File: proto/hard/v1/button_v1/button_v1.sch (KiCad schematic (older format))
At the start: 35 parts, among them J10 Conn_01x04_Male, J14 K3-2235D, J7 Conn_01x04_Female, J9 Conn_01x06_Male, Q1 TP0610T, Q3 TP0610T, Q8 IRLML2803, U1 LCD_2.8_SPI, U11 TC305, U12 LCD_1_8_SPI, U2 STM32F103C8Tx, Y1 8MHz

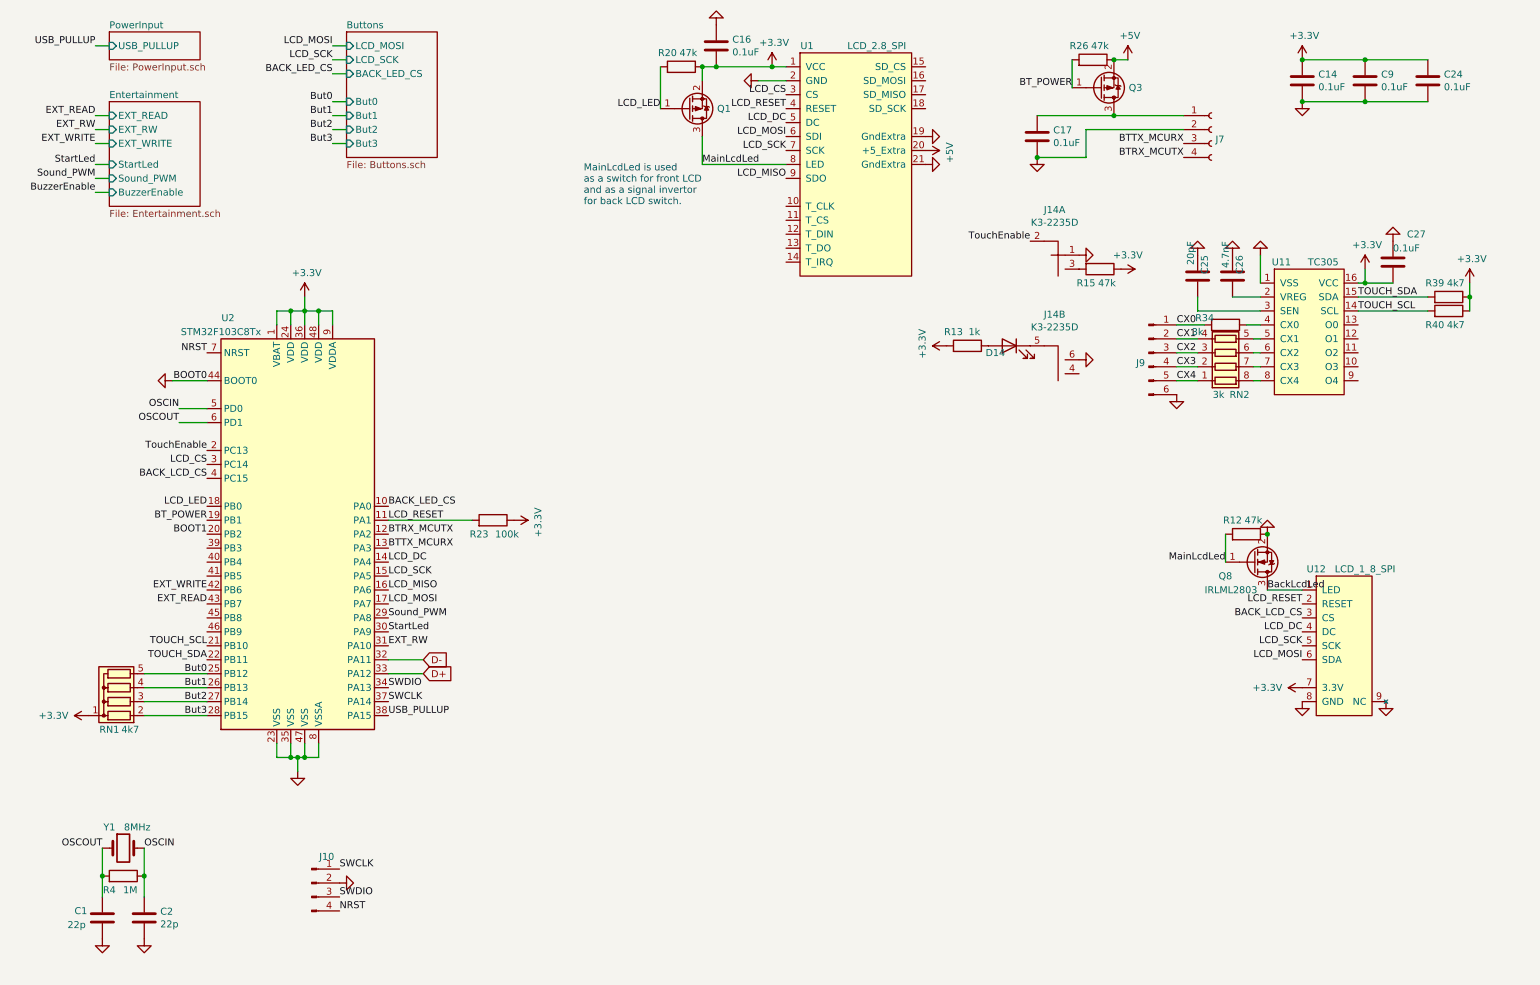
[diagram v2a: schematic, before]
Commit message: Debug connector updates: - added +3.3 connection - pins reorganized to match ST Link layout
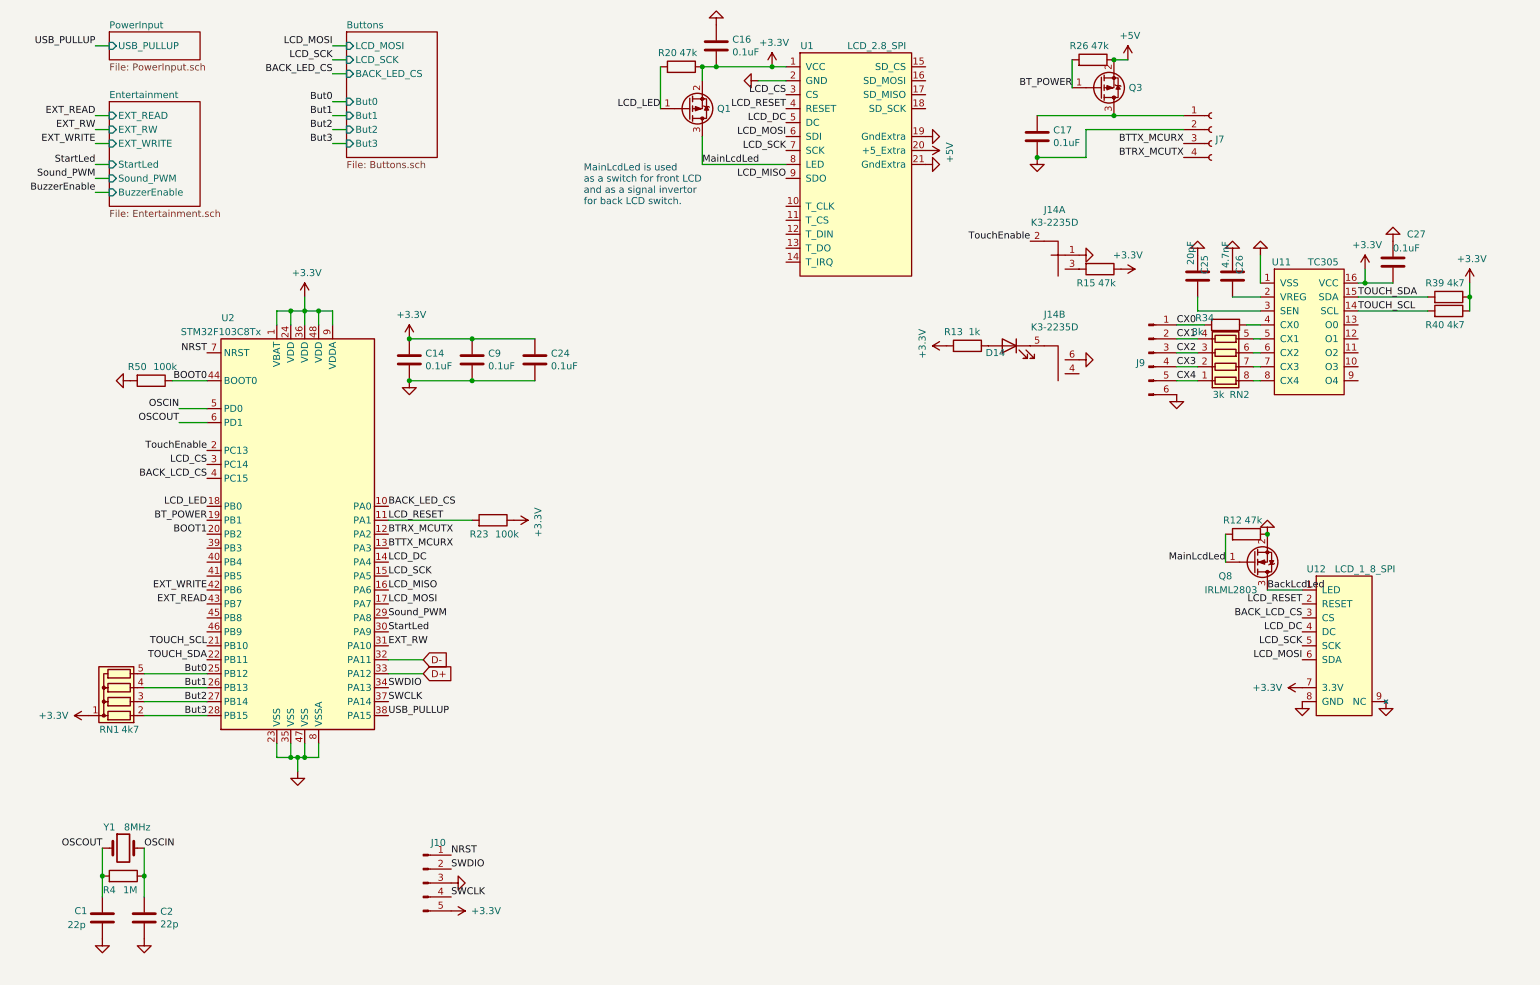
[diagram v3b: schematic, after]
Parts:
- removed J10: Conn_01x04_Male, Connector_PinHeader_2.54mm:PinHeader_1x04_P2.54mm_Vertical, symbol Connector:Conn_01x04_Male
- added J10: Conn_01x05_Male, Connector_PinHeader_2.54mm:PinHeader_1x05_P2.54mm_Vertical, symbol Connector:Conn_01x05_Male
- added R50: 100k, Resistor_SMD:R_0805_2012Metric_Pad1.15x1.40mm_HandSolder, symbol Device:R
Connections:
- net +3V3: now also J10.5 (Pin_5)
- net GND: now also J10.3 (Pin_3), R50.2; no longer U2.44 (BOOT0)
- net NRST: now also J10.1 (Pin_1)
- net SWCLK: now also J10.4 (Pin_4)
- net SWDIO: now also J10.2 (Pin_2)
- new net BOOT0: R50.1, U2.44 (BOOT0)
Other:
- moved on the sheet: C14, C24, C9
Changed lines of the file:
@@
 L power:GND #PWR036
 U 1 1 5D0E3AE6
-P 9700 1200
-F 0 "#PWR036" H 9700 950 50  0001 C CNN
-F 1 "GND" H 9705 1027 50  0001 C CNN
-F 2 "" H 9700 1200 50  0001 C CNN
-F 3 "" H 9700 1200 50  0001 C CNN
-	1    9700 1200
-	1    0    0    -1
-$EndComp
-Wire Wire Line
-	10150 1200 9700 1200
-Wire Wire Line
-	10150 1200 10600 1200
-Connection ~ 10150 1200
+P 3300 3200
+F 0 "#PWR036" H 3300 2950 50  0001 C CNN
+F 1 "GND" H 3305 3027 50  0001 C CNN
+F 2 "" H 3300 3200 50  0001 C CNN
+F 3 "" H 3300 3200 50  0001 C CNN
+	1    3300 3200
+	1    0    0    -1
+$EndComp
+Wire Wire Line
+	3750 3200 3300 3200
+Wire Wire Line
+	3750 3200 4200 3200
+Connection ~ 3750 3200
 $Comp
 L Device:C C14
 U 1 1 5D0E1987
-P 9700 1050
-F 0 "C14" H 9815 1096 50  0000 L CNN
-F 1 "0.1uF" H 9815 1005 50  0000 L CNN
-F 2 "Capacitor_SMD:C_0805_2012Metric_Pad1.15x1.40mm_HandSolder" H 9738 900 50  0001 C CNN
-F 3 "~" H 9700 1050 50  0001 C CNN
-	1    9700 1050
+P 3300 3050
+F 0 "C14" H 3415 3096 50  0000 L CNN
+F 1 "0.1uF" H 3415 3005 50  0000 L CNN
+F 2 "Capacitor_SMD:C_0805_2012Metric_Pad1.15x1.40mm_HandSolder" H 3338 2900 50  0001 C CNN
+F 3 "~" H 3300 3050 50  0001 C CNN
+	1    3300 3050
 	1    0    0    -1
 $EndComp
@@
 L power:+3.3V #PWR035
 U 1 1 5D0E374B
-P 9700 900
-F 0 "#PWR035" H 9700 750 50  0001 C CNN
-F 1 "+3.3V" H 9715 1073 50  0000 C CNN
-F 2 "" H 9700 900 50  0001 C CNN
-F 3 "" H 9700 900 50  0001 C CNN
-	1    9700 900
+P 3300 2900
+F 0 "#PWR035" H 3300 2750 50  0001 C CNN
+F 1 "+3.3V" H 3315 3073 50  0000 C CNN
+F 2 "" H 3300 2900 50  0001 C CNN
+F 3 "" H 3300 2900 50  0001 C CNN
+	1    3300 2900
 	1    0    0    -1
 $EndComp
@@
 L Device:C C9
 U 1 1 5D0DBD3D
-P 10150 1050
-F 0 "C9" H 10265 1096 50  0000 L CNN
-F 1 "0.1uF" H 10265 1005 50  0000 L CNN
-F 2 "Capacitor_SMD:C_0805_2012Metric_Pad1.15x1.40mm_HandSolder" H 10188 900 50  0001 C CNN
-F 3 "~" H 10150 1050 50  0001 C CNN
-	1    10150 1050
-	1    0    0    -1
-$EndComp
-Wire Wire Line
-	10150 900  9700 900
+P 3750 3050
+F 0 "C9" H 3865 3096 50  0000 L CNN
+F 1 "0.1uF" H 3865 3005 50  0000 L CNN
+F 2 "Capacitor_SMD:C_0805_2012Metric_Pad1.15x1.40mm_HandSolder" H 3788 2900 50  0001 C CNN
+F 3 "~" H 3750 3050 50  0001 C CNN
+	1    3750 3050
+	1    0    0    -1
+$EndComp
+Wire Wire Line
+	3750 2900 3300 2900
 $Comp
 L Device:C C24
 U 1 1 5D604E60
-P 10600 1050
-F 0 "C24" H 10715 1096 50  0000 L CNN
-F 1 "0.1uF" H 10715 1005 50  0000 L CNN
-F 2 "Capacitor_SMD:C_0805_2012Metric_Pad1.15x1.40mm_HandSolder" H 10638 900 50  0001 C CNN
-F 3 "~" H 10600 1050 50  0001 C CNN
-	1    10600 1050
-	1    0    0    -1
-$EndComp
-Wire Wire Line
-	10600 900  10150 900
-Connection ~ 10150 900
+P 4200 3050
+F 0 "C24" H 4315 3096 50  0000 L CNN
+F 1 "0.1uF" H 4315 3005 50  0000 L CNN
+F 2 "Capacitor_SMD:C_0805_2012Metric_Pad1.15x1.40mm_HandSolder" H 4238 2900 50  0001 C CNN
+F 3 "~" H 4200 3050 50  0001 C CNN
+	1    4200 3050
+	1    0    0    -1
+$EndComp
+Wire Wire Line
+	4200 2900 3750 2900
+Connection ~ 3750 2900
 $Comp
 L Connector:Conn_01x04_Female J7
@@
 F2 "USB_PULLUP" I L 1150 800 50
 $EndSheet
-Connection ~ 9700 900
-Connection ~ 9700 1200
+Connection ~ 3300 2900
+Connection ~ 3300 3200
 Text Label 3150 4100 0    50   ~ 0
 BACK_LED_CS
@@
 Wire Wire Line
 	1050 1850 1150 1850
-Text Label 2800 7000 0    50   ~ 0
+Text Label 3600 6600 0    50   ~ 0
 NRST
-Text Label 2800 6700 0    50   ~ 0
+Text Label 3600 6900 0    50   ~ 0
 SWCLK
-Text Label 2800 6900 0    50   ~ 0
+Text Label 3600 6700 0    50   ~ 0
 SWDIO
 $Comp
 L power:GND #PWR0139
 U 1 1 5D4D063C
-P 2800 6800
-F 0 "#PWR0139" H 2800 6550 50  0001 C CNN
-F 1 "GND" H 2805 6627 50  0001 C CNN
-F 2 "" H 2800 6800 50  0001 C CNN
-F 3 "" H 2800 6800 50  0001 C CNN
-	1    2800 6800
+P 3600 6800
+F 0 "#PWR0139" H 3600 6550 50  0001 C CNN
+F 1 "GND" H 3605 6627 50  0001 C CNN
+F 2 "" H 3600 6800 50  0001 C CNN
+F 3 "" H 3600 6800 50  0001 C CNN
+	1    3600 6800
 	0    -1   -1   0
 $EndComp
@@
 	1    8400 2400
 	0    1    1    0
-$EndComp
-$Comp
-L Connector:Conn_01x04_Male J10
-U 1 1 5D6C6312
-P 2600 6800
-F 0 "J10" H 2708 6989 50  0000 C CNN
-F 1 "Conn_01x04_Male" H 2708 6990 50  0001 C CNN
-F 2 "Connector_PinHeader_2.54mm:PinHeader_1x04_P2.54mm_Vertical" H 2600 6800 50  0001 C CNN
-F 3 "~" H 2600 6800 50  0001 C CNN
-	1    2600 6800
-	1    0    0    -1
 $EndComp
 $Comp
@@
 L power:GND #PWR0168
 U 1 1 5F134F3D
-P 1600 3200
-F 0 "#PWR0168" H 1600 2950 50  0001 C CNN
-F 1 "GND" H 1605 3027 50  0001 C CNN
-F 2 "" H 1600 3200 50  0001 C CNN
-F 3 "" H 1600 3200 50  0001 C CNN
-	1    1600 3200
+P 1300 3200
+F 0 "#PWR0168" H 1300 2950 50  0001 C CNN
+F 1 "GND" H 1305 3027 50  0001 C CNN
+F 2 "" H 1300 3200 50  0001 C CNN
+F 3 "" H 1300 3200 50  0001 C CNN
+	1    1300 3200
 	0    1    1    0
 $EndComp
@@
 Text Label 9150 4500 2    50   ~ 0
 MainLcdLed
+$Comp
+L Device:R R50
+U 1 1 5F13C9FC
+P 1450 3200
+F 0 "R50" V 1350 3100 50  0000 C CNN
+F 1 "100k" V 1350 3300 50  0000 C CNN
+F 2 "Resistor_SMD:R_0805_2012Metric_Pad1.15x1.40mm_HandSolder" V 1380 3200 50  0001 C CNN
+F 3 "~" H 1450 3200 50  0001 C CNN
+	1    1450 3200
+	0    1    1    0
+$EndComp
+$Comp
+L Connector:Conn_01x05_Male J10
+U 1 1 5F1D58E0
+P 3400 6800
+F 0 "J10" H 3508 7089 50  0000 C CNN
+F 1 "Conn_01x05_Male" H 3508 7090 50  0001 C CNN
+F 2 "Connector_PinHeader_2.54mm:PinHeader_1x05_P2.54mm_Vertical" H 3400 6800 50  0001 C CNN
+F 3 "~" H 3400 6800 50  0001 C CNN
+	1    3400 6800
+	1    0    0    -1
+$EndComp
+$Comp
+L power:+3.3V #PWR0169
+U 1 1 5F1D7298
+P 3600 7000
+F 0 "#PWR0169" H 3600 6850 50  0001 C CNN
+F 1 "+3.3V" V 3600 7250 50  0000 C CNN
+F 2 "" H 3600 7000 50  0001 C CNN
+F 3 "" H 3600 7000 50  0001 C CNN
+	1    3600 7000
+	0    1    1    0
+$EndComp
 $EndSCHEMATC

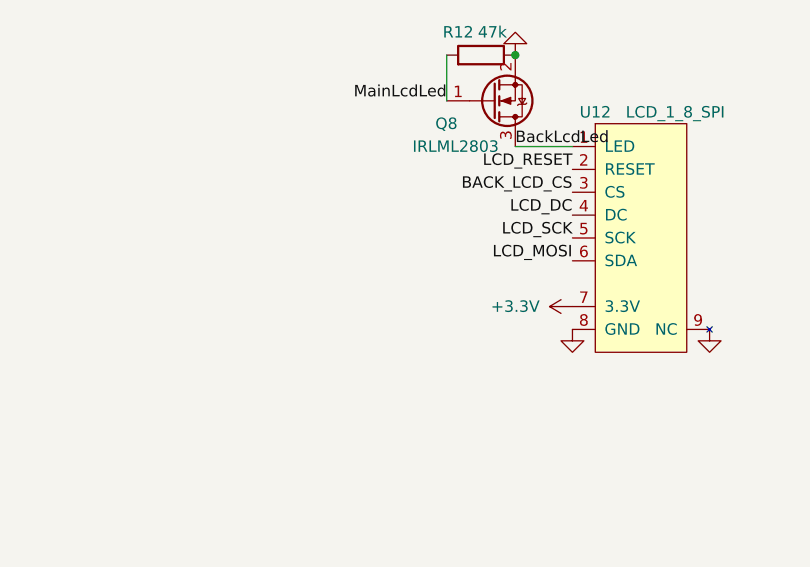
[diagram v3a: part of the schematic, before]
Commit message: Added cap for back LCD. Modified traces to optimize power distribution.
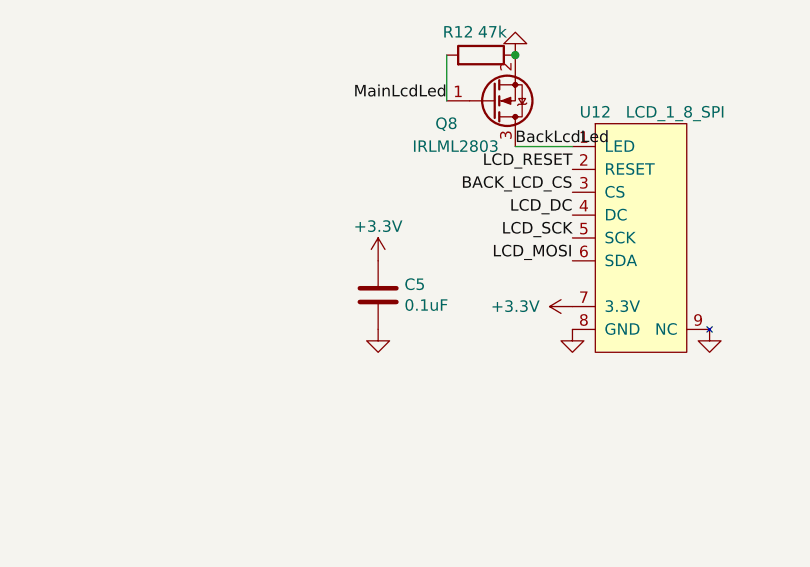
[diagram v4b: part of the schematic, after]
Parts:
- added C5: 0.1uF, Capacitor_SMD:C_0805_2012Metric_Pad1.15x1.40mm_HandSolder, symbol Device:C
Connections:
- net +3V3: now also C5.1
- net GND: now also C5.2
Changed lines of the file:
@@
 	0    1    1    0
 $EndComp
+$Comp
+L Device:C C5
+U 1 1 5F20E3F6
+P 8850 5350
+F 0 "C5" H 8965 5396 50  0000 L CNN
+F 1 "0.1uF" H 8965 5305 50  0000 L CNN
+F 2 "Capacitor_SMD:C_0805_2012Metric_Pad1.15x1.40mm_HandSolder" H 8888 5200 50  0001 C CNN
+F 3 "~" H 8850 5350 50  0001 C CNN
+	1    8850 5350
+	1    0    0    -1
+$EndComp
+$Comp
+L power:GND #PWR0170
+U 1 1 5F20F286
+P 8850 5500
+F 0 "#PWR0170" H 8850 5250 50  0001 C CNN
+F 1 "GND" H 8855 5327 50  0001 C CNN
+F 2 "" H 8850 5500 50  0001 C CNN
+F 3 "" H 8850 5500 50  0001 C CNN
+	1    8850 5500
+	1    0    0    -1
+$EndComp
+$Comp
+L power:+3.3V #PWR0171
+U 1 1 5F20F54B
+P 8850 5200
+F 0 "#PWR0171" H 8850 5050 50  0001 C CNN
+F 1 "+3.3V" H 8850 5350 50  0000 C CNN
+F 2 "" H 8850 5200 50  0001 C CNN
+F 3 "" H 8850 5200 50  0001 C CNN
+	1    8850 5200
+	1    0    0    -1
+$EndComp
 $EndSCHEMATC
